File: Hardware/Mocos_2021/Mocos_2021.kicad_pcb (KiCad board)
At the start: 2 copper layers, 124.5 x 24.9 mm, 104 parts, among them IC1 TC2117, J1 USB_B_Mini, J2 SERIAL PORT, J3 Programming, Q1 IRFS7530, Q2 IRFS7530, Q3 IRFS7530, Q4 IRFS7530, Q5 IRFS7530, Q6 IRFS7530, U1 DRV8302, U2 STM32F40X_LQFP64, X1 8MHz, 10ppm

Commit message: Finished STM32 Layout
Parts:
- removed Conn3: Phase2, MRDT_Connectors:Anderson_2_Horizontal_Side_by_Side
- removed Conn4: Phase3, MRDT_Connectors:Anderson_2_Horizontal_Side_by_Side
- removed R7: 0, Resistor_SMD:R_0603_1608Metric_Pad0.98x0.95mm_HandSolder
- C1: value 2.2u -> 2.2u 16V
- C11: value 6.8n -> 6.8n, 50V
- C13, C16: moved to B.Cu
- C17: value 22n -> 22n, 50V
- C2, C39: value 100n -> 100n, 50V
- C38: value 15p -> 15p, 50V
- C4: value 2.2u -> 2.2u, 6V
- C7: value 100u -> 100u, 6V
- Conn1: footprint MRDT_Connectors:Anderson_2_Vertical_Sidy_by_Side -> MRDT_Connectors:Anderson_2_Horizontal_Side_by_Side_PV
- Conn2: value Phase1 -> Phases; footprint MRDT_Connectors:Anderson_2_Horizontal_Side_by_Side -> MRDT_Connectors:Anderson_3_Horizontal_Side_by_Side
- IC1: footprint v-reg-78XXS -> crf1:SOT-223
- J1: footprint crf1:mini_USB_gnd -> crf1:USB-UX60R-MB-5ST
- J2: footprint MRDT_Connectors:MOLEX_uF_S_03_Vertical -> MRDT_Connectors:MOLEX_uF_S_03_Horizontal
- J3: footprint MRDT_Connectors:MOLEX_uF_S_05_Vertical -> MRDT_Connectors:MOLEX_uF_S_05_Horizontal
- Q1, Q2, Q5, Q6: value IRFS7530 -> IRFZ44ESTRLPBF; footprint Package_TO_SOT_SMD:TO-263-7_TabPin4 -> Package_TO_SOT_SMD:TO-263-3_TabPin4
- Q3, Q4: value IRFS7530 -> IRFZ44ESTRLPBF; footprint Package_TO_SOT_SMD:TO-263-7_TabPin4 -> Package_TO_SOT_SMD:TO-263-3_TabPin4; moved to B.Cu
- R20, R21, R22, R23: value 100K -> 100; moved to B.Cu
- moved R32 124.7 mm to (73.8, 101.2)
- moved R29 106.9 mm to (80.6, 100.5)
- moved R34 96.1 mm to (68.2, 99.9)
- moved R35 94.7 mm to (89.1, 100.3)
- moved R11 94.3 mm to (98.2, 84.1), turned to 270 degrees
- moved R10 89.9 mm to (106.4, 77.8), turned to 90 degrees
- moved C23 88.3 mm to (105.0, 87.0), turned to 90 degrees
- moved C4 87.3 mm to (109.0, 76.0), turned to 90 degrees
- moved C6 86.6 mm to (182.6, 108.2), turned to 90 degrees
- moved Q1 85.1 mm to (115.4, 112.3)
- moved R37 83.2 mm to (85.4, 97.2)
- moved C25 80.9 mm to (119.9, 89.0), turned to 270 degrees
- moved J2 77.9 mm to (150.6, 78.1)
- moved R25 73.7 mm to (114.2, 94.7), turned to 180 degrees
- moved C30 73.6 mm to (145.5, 81.9)
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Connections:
- net USB_DM renamed USB-
- net USB_DP renamed USB+
- Conn2 pad 1: H2_LOW -> H1_VS
- Conn2 pad 2: (no net) -> H2_VS
- X1 pad 2: Net-(C38-Pad1) -> H2_LOW
- X1 pad 3: H2_LOW -> Net-(C38-Pad1)
- X1 pad 4: (no net) -> H2_LOW
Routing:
- net +3V3: track 0.00 -> 167.0 mm, vias 0 -> 11
- net Net-(C19-Pad1): track 0.00 -> 56.2 mm, vias 0 -> 2
- net Net-(J3-Pad2): track 0.00 -> 55.0 mm, vias 0 -> 3
- net VDD: track 0.00 -> 50.4 mm, vias 0 -> 2
- net Net-(J3-Pad4): track 0.00 -> 41.5 mm, vias 0 -> 1
- net +5V: track 0.00 -> 39.4 mm
- net H2_LOW: track 0.00 -> 37.4 mm, vias 0 -> 22
- net Net-(C39-Pad1): track 0.00 -> 26.0 mm
- net BR_SO2: track 0.00 -> 25.4 mm, vias 0 -> 2
- net DC_CAL: track 0.00 -> 24.2 mm, vias 0 -> 2
- net AN_IN: track 0.00 -> 24.1 mm, vias 0 -> 2
- net Net-(C38-Pad1): track 0.00 -> 23.8 mm, vias 0 -> 2
- net BR_SO1: track 0.00 -> 23.3 mm, vias 0 -> 4
- net TX_SDA_NSS: track 0.00 -> 22.5 mm, vias 0 -> 2
- net RX_SCL_MOSI: track 0.00 -> 22.0 mm, vias 0 -> 2
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- added copper zone on B.Cu, net H2_LOW
- added copper zone on F.Cu, net H2_LOW
- added copper zone on B.Cu, net VDD
- added copper zone on F.Cu, net VDD
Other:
- board size 124.5 x 24.9 mm -> 124.5 x 86.1 mm

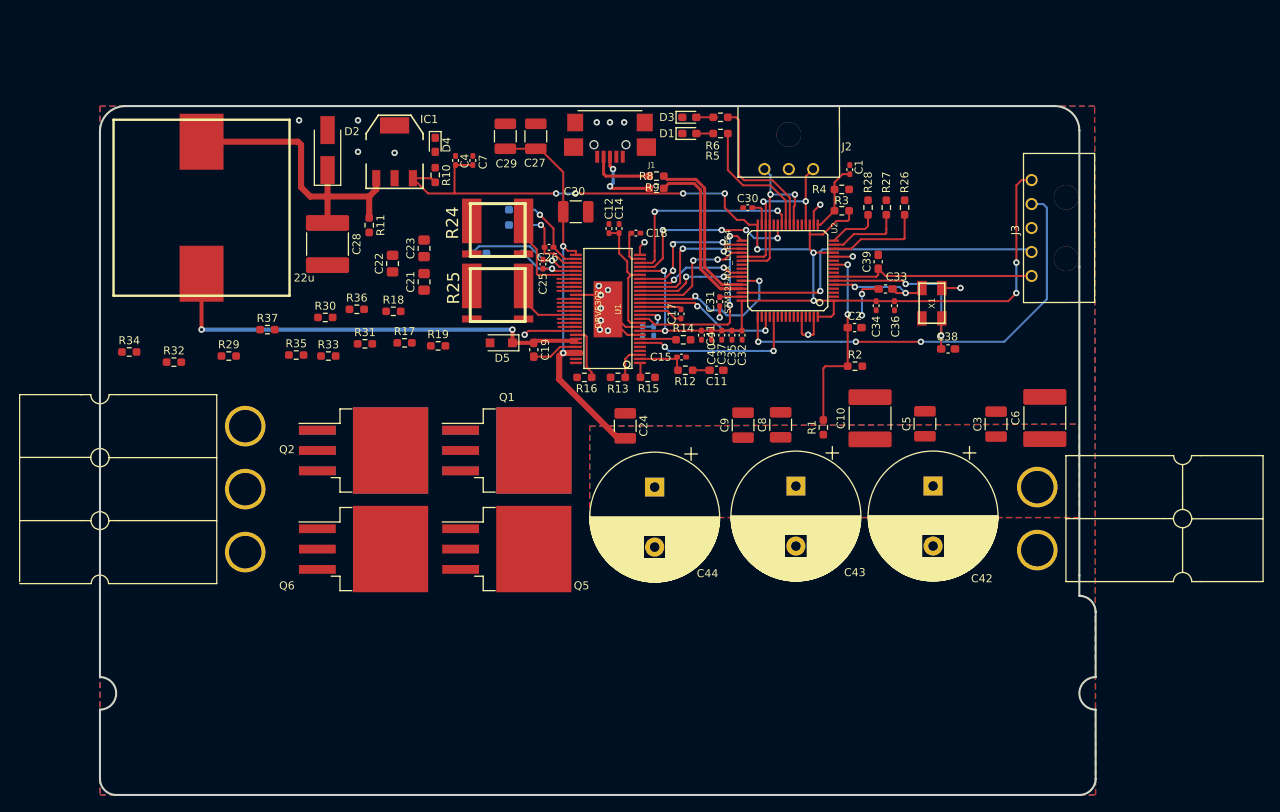
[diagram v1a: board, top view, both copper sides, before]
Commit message: Added 3.3V Oki for cleaner layout
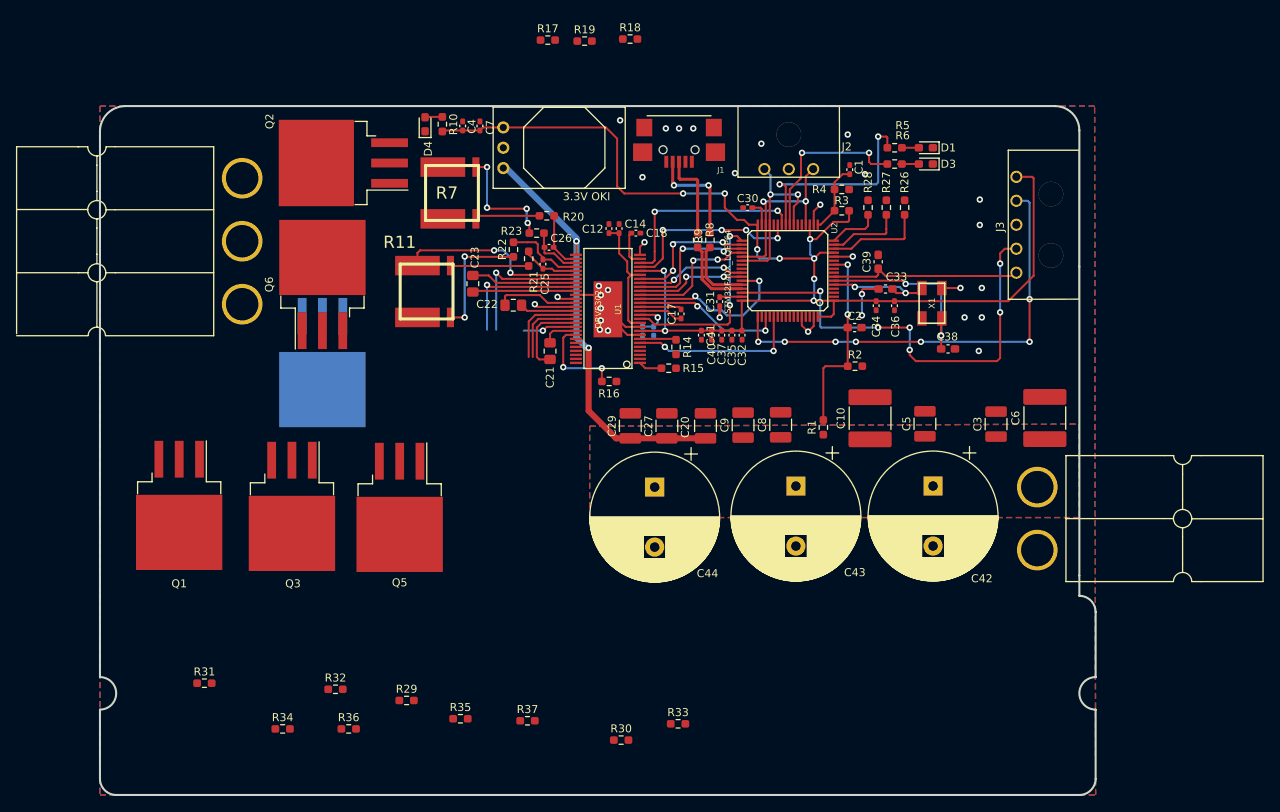
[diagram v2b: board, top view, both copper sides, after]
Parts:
- removed C11: 6.8n, 50V, Capacitor_SMD:C_0603_1608Metric_Pad1.08x0.95mm_HandSolder
- removed C15: 120p, Capacitor_SMD:C_0402_1005Metric_Pad0.74x0.62mm_HandSolder
- removed C19: 100n, Capacitor_SMD:C_0603_1608Metric_Pad1.08x0.95mm_HandSolder
- removed C24: 10u,50V, Capacitor_SMD:C_1210_3225Metric_Pad1.33x2.70mm_HandSolder
- removed C28: 100u, Capacitor_SMD:C_2220_5650Metric_Pad1.97x5.40mm_HandSolder
- removed D2: TVS_5V, Diode_SMD:D_SMA_Handsoldering
- removed D5: 60V,2A, Diode_SMD:D_SOD-123F
- removed IC1: TC2117, crf1:SOT-223
- removed L1: 22u, crf1:inductor_74435580680
- removed R12: 15K, Resistor_SMD:R_0603_1608Metric_Pad0.98x0.95mm_HandSolder
- removed R13: 3.3K, Resistor_SMD:R_0603_1608Metric_Pad0.98x0.95mm_HandSolder
- removed R24, R25: 1m, crf1:WSLP2726
- added R7: 1m, crf1:WSLP2726, F.Cu at (110.4, 80.1)
- added U3: 3.3V OKI, MRDT_Devices:OKI_Horizontal, F.Cu at (114.9, 77.0)
- Q1, Q2, Q4, Q5, Q6: footprint Package_TO_SOT_SMD:TO-263-3_TabPin4 -> MRDT_Actives:IRFZ44ESTRLPBF
- Q3: footprint Package_TO_SOT_SMD:TO-263-3_TabPin4 -> MRDT_Actives:IRFZ44ESTRLPBF; moved to F.Cu
- R11: value 18K -> 1m; footprint Resistor_SMD:R_0603_1608Metric_Pad0.98x0.95mm_HandSolder -> crf1:WSLP2726
- R20, R21, R22, R23: moved to F.Cu
- moved R30 64.5 mm to (129.7, 148.5)
- moved R33 63.4 mm to (136.8, 146.4)
- moved R37 58.7 mm to (118.0, 146.1)
- moved R36 52.5 mm to (95.6, 147.1)
- moved R34 50.9 mm to (87.4, 147.1)
- moved R35 49.9 mm to (109.6, 145.8)
- moved R29 48.5 mm to (102.8, 143.5)
- moved R31 46.9 mm to (77.6, 141.4)
- moved R32 45.6 mm to (94.0, 142.1)
- moved R18 45.1 mm to (130.8, 60.8)
- moved R19 42.3 mm to (125.1, 61.1)
- moved R17 41.9 mm to (120.5, 61.0)
- moved Q1 41.5 mm to (74.4, 119.1), turned to 270 degrees
- moved C27 39.7 mm to (135.4, 109.2)
- moved C29 39.4 mm to (130.8, 109.2)
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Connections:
- J1 pad 1: Net-(J1-Pad1) -> (no net)
- J1 pad 4: Net-(J1-Pad4) -> (no net)
- R11 pad 1: +5V -> H3_LOW
- R11 pad 2: Net-(R11-Pad2) -> H2_LOW
- R20 pad 1: H2_LOW -> Net-(R20-Pad1)
- R21 pad 1: H3_LOW -> Net-(R11-Pad3)
- R22 pad 1: H2_LOW -> Net-(R11-Pad4)
- R23 pad 1: H1_LOW -> Net-(R23-Pad1)
- U1 pad 2: Net-(C15-Pad1) -> (no net)
- U1 pad 3: Net-(R11-Pad2) -> (no net)
- U1 pad 4: Net-(U1-Pad4) -> (no net)
- U1 pad 5: Net-(U1-Pad5) -> (no net)
- U1 pad 50: Net-(C19-Pad1) -> (no net)
- U1 pad 51: Net-(C19-Pad1) -> (no net)
- U1 pad 52: Net-(C19-Pad2) -> (no net)
- U1 pad 53: VDD -> (no net)
- U1 pad 54: VDD -> (no net)
- U1 pad 55: Net-(U1-Pad55) -> (no net)
- U1 pad 56: Net-(U1-Pad56) -> (no net)
- U2 pad 11: Net-(U2-Pad11) -> (no net)
- U2 pad 2: Net-(U2-Pad2) -> (no net)
- U2 pad 21: SCK_ADC_EXT -> (no net)
- U2 pad 22: MISO_ADC_EXT2 -> (no net)
- U2 pad 28: Net-(U2-Pad28) -> (no net)
- U2 pad 3: Net-(U2-Pad3) -> (no net)
- U2 pad 39: Net-(U2-Pad39) -> (no net)
- U2 pad 4: Net-(U2-Pad4) -> (no net)
- U2 pad 40: Net-(U2-Pad40) -> (no net)
- U2 pad 50: Net-(U2-Pad50) -> (no net)
- U2 pad 52: HALL_3 -> (no net)
- U2 pad 54: Net-(U2-Pad54) -> (no net)
- U2 pad 55: Net-(U2-Pad55) -> (no net)
- U2 pad 56: Net-(U2-Pad56) -> (no net)
- U2 pad 57: SERVO -> (no net)
- U2 pad 58: HALL_1 -> (no net)
- U2 pad 59: HALL_2 -> (no net)
- U2 pad 61: CAN_RX -> (no net)
- U2 pad 62: CAN_TX -> (no net)
- U2 pad 8: TEMP_MOTOR -> (no net)
- U2 pad 9: Net-(U2-Pad9) -> (no net)
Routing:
- net Net-(C19-Pad1): track 56.2 -> 0.00 mm, vias 2 -> 0
- net +5V: track 39.4 -> 0.00 mm
- net Net-(R11-Pad4): track 0.00 -> 15.5 mm, vias 0 -> 2
- net M_L3: track 2.34 -> 17.4 mm, vias 0 -> 1
- net Net-(J3-Pad4): track 41.5 -> 56.2 mm, vias 1 -> 6
- net Net-(R23-Pad1): track 0.00 -> 14.7 mm, vias 0 -> 4
- net M_H3: track 2.34 -> 16.8 mm, vias 0 -> 1
- net USB-: track 21.2 -> 8.80 mm
- net H3_LOW: track 12.2 -> 23.9 mm, vias 0 -> 2
- net USB+: track 21.2 -> 9.67 mm
- net H3_VS: track 2.35 -> 13.3 mm
- net Net-(C23-Pad2): track 2.33 -> 13.0 mm
- net LED_RED: track 16.4 -> 26.3 mm, vias 0 -> 2
- net Net-(R11-Pad3): track 0.00 -> 9.80 mm
- net H1_VS: track 2.27 -> 10.6 mm
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
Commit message: Retraced the entire VDD Net and readjusted the Mosfet placement
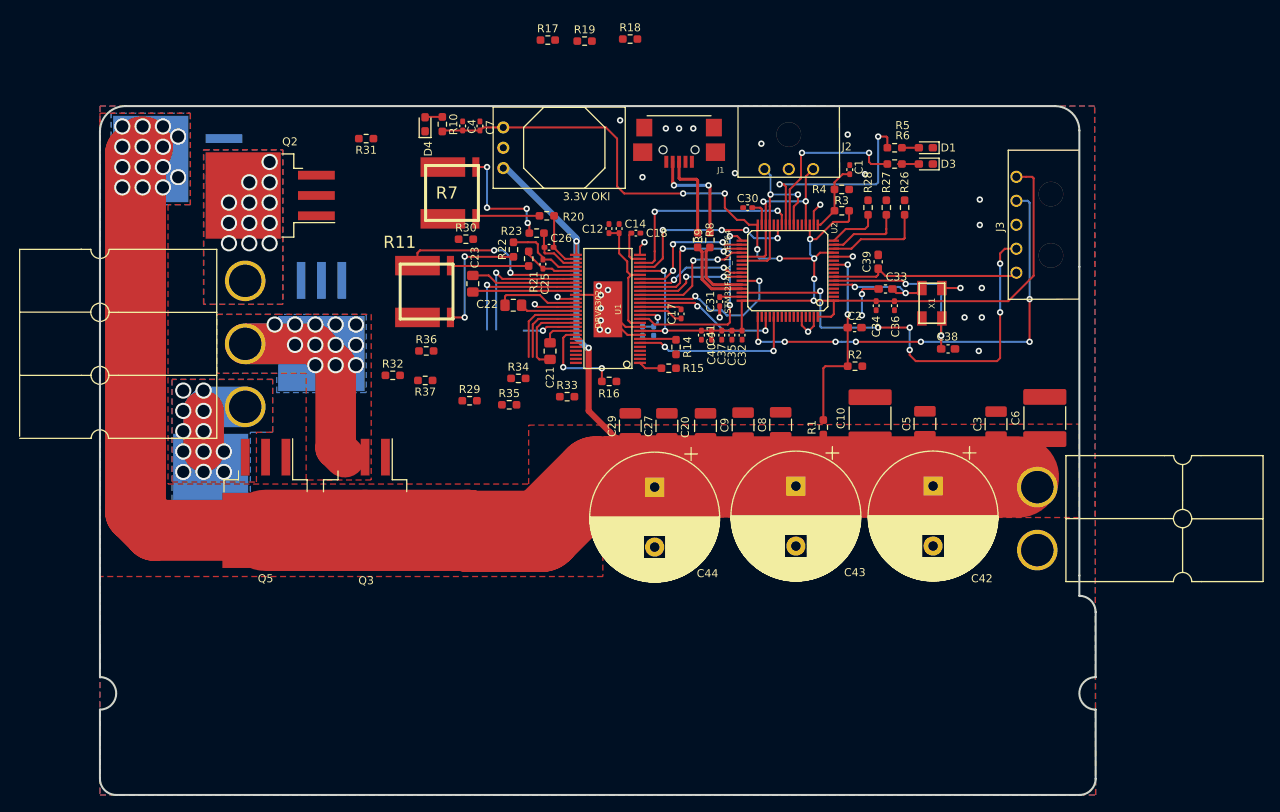
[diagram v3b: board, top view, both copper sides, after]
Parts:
- Q1, Q6: moved to B.Cu
- moved R31 71.0 mm to (97.8, 73.3), turned to 180 degrees
- moved R30 65.5 mm to (110.3, 85.9)
- moved R34 52.8 mm to (116.8, 103.3)
- moved R36 48.2 mm to (105.3, 99.8)
- moved R37 44.4 mm to (105.2, 103.5), turned to 180 degrees
- moved Q1 43.3 mm to (74.2, 75.8), turned to 180 degrees
- moved R33 43.2 mm to (122.9, 105.5)
- moved R32 39.9 mm to (101.1, 102.9)
- moved R35 39.7 mm to (115.7, 106.6)
- moved R29 38.3 mm to (110.7, 106.0)
- moved Q6 29.7 mm to (75.0, 115.6), turned to 0 degrees
- moved Q5 16.8 mm to (85.2, 118.9)
- moved Conn2 12.8 mm to (82.7, 91.1)
- moved Q2 10.0 mm to (85.8, 80.4)
- moved Q3 9.15 mm to (97.7, 118.9)
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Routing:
- net VDD: track 52.9 -> 213.1 mm, vias 2 -> 16
- net H2_VS: track 10.4 -> 46.2 mm, vias 0 -> 12
- net H3_VS: track 13.3 -> 32.4 mm, vias 0 -> 12
- net H1_VS: vias 0 -> 12
- added copper zone on B.Cu, net H1_VS
- added copper zone on F.Cu, net H1_VS
- added copper zone on B.Cu, net H2_VS
- added copper zone on F.Cu, net H2_VS
- added copper zone on B.Cu, net H3_VS
- added copper zone on F.Cu, net H3_VS

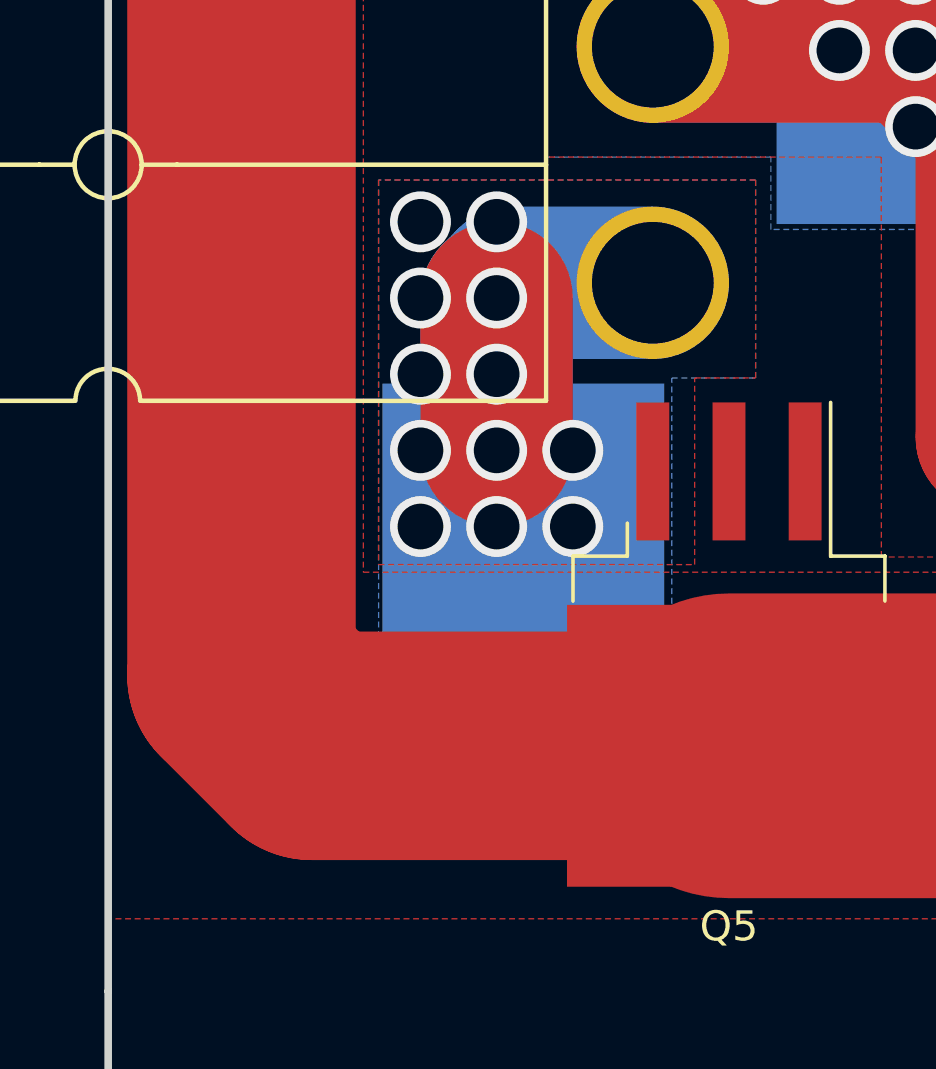
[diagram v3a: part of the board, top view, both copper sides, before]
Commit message: Moved Q6 to a better position for Routing
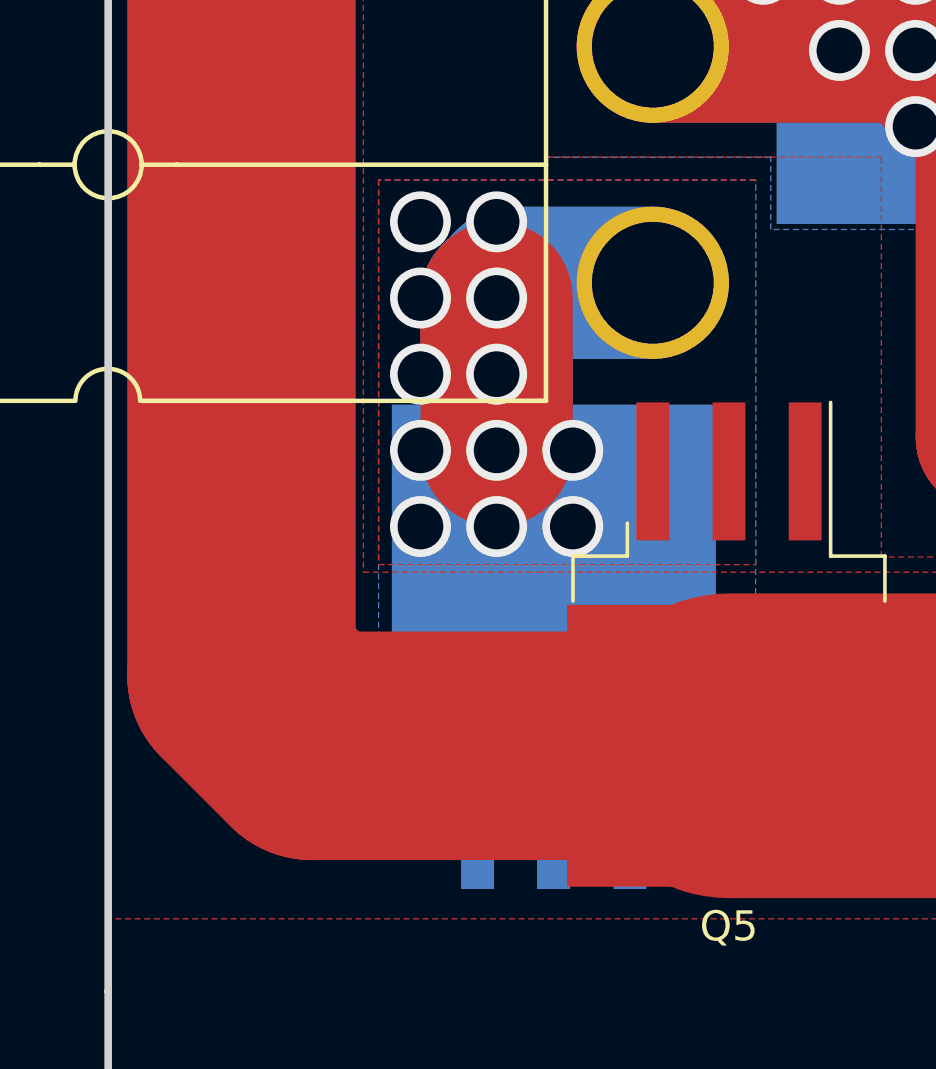
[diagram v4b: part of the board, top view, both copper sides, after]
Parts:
- moved Q6 5.54 mm to (79.4, 118.9), turned to 90 degrees
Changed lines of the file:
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@@
   )
   (module MRDT_Actives:IRFZ44ESTRLPBF (layer B.Cu)
-    (at 74.984 115.57)
+    (at 79.375 118.945 90)
     (descr "TO-263 / D2PAK / DDPAK SMD package, http://www.infineon.com/cms/en/product/packages/PG-TO263/PG-TO263-3-1/")
     (tags "D2PAK DDPAK TO-263 D2PAK-3 TO-263-3 SOT-404")
     (attr smd)
-    (fp_text reference Q6 (at 0 6.65 180) (layer B.SilkS)
+    (fp_text reference Q6 (at 0 6.65 270) (layer B.SilkS)
       (effects (font (size 1 1) (thickness 0.15)) (justify mirror))
     )
-    (fp_text value IRFZ44ESTRLPBF (at 0 -6.65 180) (layer B.Fab)
+    (fp_text value IRFZ44ESTRLPBF (at 0 -6.65 270) (layer B.Fab)
       (effects (font (size 1 1) (thickness 0.15)) (justify mirror))
     )
@@
     (fp_line (start 8.32 -5.65) (end 8.32 5.65) (layer B.CrtYd) (width 0.05))
     (fp_line (start 8.32 5.65) (end -8.32 5.65) (layer B.CrtYd) (width 0.05))
-    (fp_text user %R (at 0 0 180) (layer B.Fab)
+    (fp_text user %R (at 0 0 270) (layer B.Fab)
       (effects (font (size 1 1) (thickness 0.15)) (justify mirror))
     )
-    (pad 2 smd rect (at -5.775 2.54) (size 4.600001 1.1) (layers B.Cu B.Paste B.Mask)
+    (pad 2 smd rect (at -5.775 2.54 90) (size 4.600001 1.1) (layers B.Cu B.Paste B.Mask)
       (net 42 "Net-(Q6-Pad2)"))
-    (pad "" smd rect (at -5.775 0) (size 4.600001 1.1) (layers B.Cu B.Paste B.Mask))
-    (pad 3 smd rect (at -5.775 -2.54) (size 4.6 1.1) (layers B.Cu B.Paste B.Mask)
+    (pad "" smd rect (at -5.775 0 90) (size 4.600001 1.1) (layers B.Cu B.Paste B.Mask))
+    (pad 3 smd rect (at -5.775 -2.54 90) (size 4.6 1.1) (layers B.Cu B.Paste B.Mask)
       (net 41 H3_LOW))
-    (pad 1 smd rect (at 3.375 0) (size 9.399999 10.800001) (layers B.Cu B.Paste B.Mask)
+    (pad 1 smd rect (at 3.375 0 90) (size 9.399999 10.800001) (layers B.Cu B.Paste B.Mask)
       (net 16 H3_VS))
     (model ${KISYS3DMOD}/Package_TO_SOT_SMD.3dshapes/TO-263-3_TabPin2.wrl
@@
     (polygon
       (pts
-        (xy 84.074 116.205) (xy 84.074 109.982) (xy 86.106 109.982) (xy 86.106 103.378) (xy 73.533 103.378)
-        (xy 73.533 116.205)
+        (xy 86.106 116.205) (xy 86.106 103.378) (xy 73.533 103.378) (xy 73.533 116.205)
       )
     )
@@
     (polygon
       (pts
-        (xy 83.312 121.031) (xy 83.312 109.982) (xy 86.106 109.982) (xy 86.106 103.378) (xy 73.533 103.378)
-        (xy 73.533 121.031)
+        (xy 86.106 121.031) (xy 86.106 103.378) (xy 73.533 103.378) (xy 73.533 121.031)
       )
     )
